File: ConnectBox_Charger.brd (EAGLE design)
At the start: 65 x 30 mm, 1 part, among them J1 CONNECTOR_PI_40_PIN

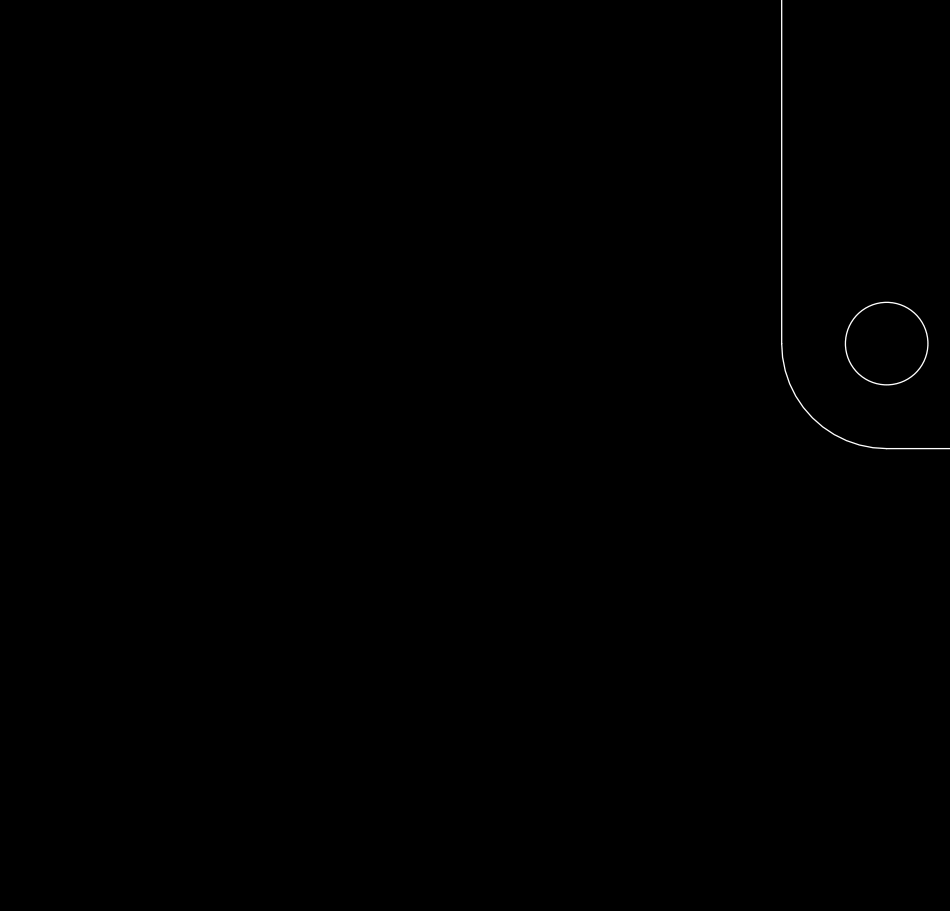
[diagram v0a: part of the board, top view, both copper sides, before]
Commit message: Add LTC4040 Breakout
Breakout from an Analog Devices/Linear Technology LTC4040 “2.5A Battery Backup Power Manager” IC. Boost SMPS with 5V out, and buck SMPS to charge lithium cell. Li-Ion selectable 3.95V/4.0V/4.05V/4.1V Lithium Iron Phosphate LiFePO4 selectable 3.45V/3.5V/3.55V/3.6V

https://www.analog.com/en/products/ltc4040.html
https://www.analog.com/media/en/technical-documentation/data-sheets/4040fb.pdf

Package UFD, QFN 4mm x 5mm. 24 pins plus Exposed Pad. LTC4040EUFD
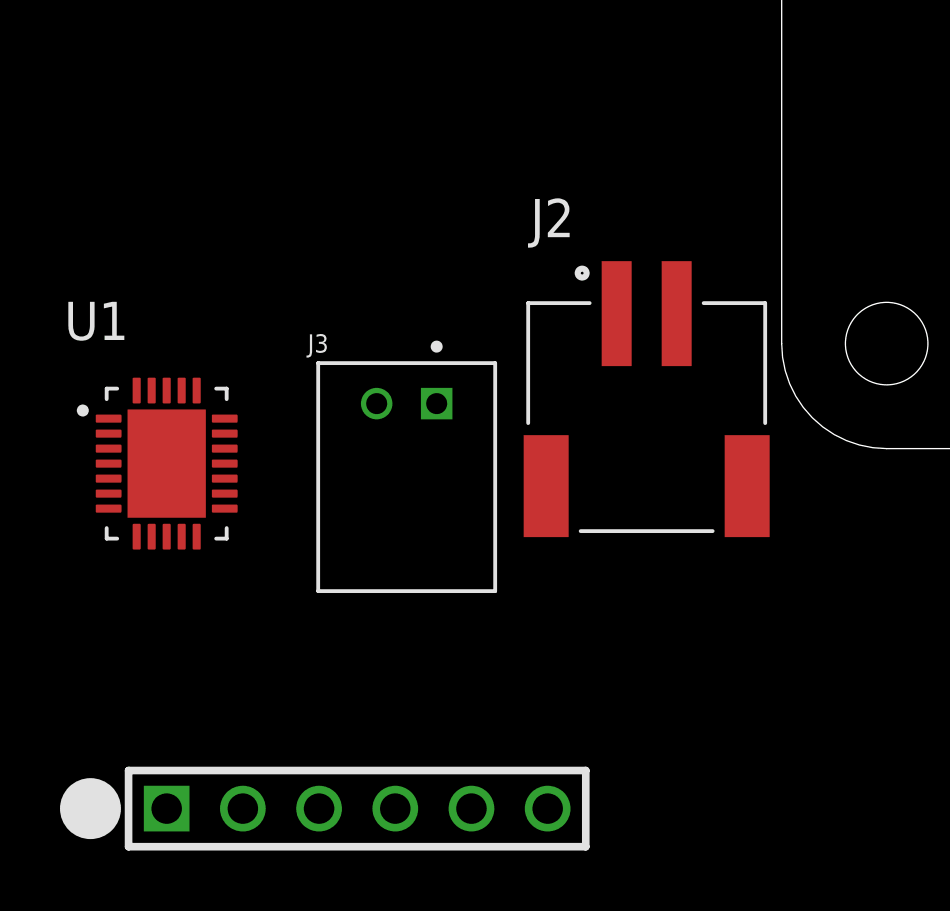
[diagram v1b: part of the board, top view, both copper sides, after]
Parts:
- added J2: JST-2 SMT, ConnectBox_2019:JST_S2B-PH-SM4-TB(LF)(SN)
- added J3: JST-2 TH, ConnectBox_2019:JST_S2B-PH-K-S(LF)(SN)
- added J4: CONNECTOR-6-FTDI, ConnectBox_2019:ESQ-106-XX-X-S
- added U1: LTC4040, ConnectBox_2019:QFN50P500X400X80-25N
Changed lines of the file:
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@@
 <attribute name="VALUE" x="7.1" y="22.055" size="1.27" layer="27"/>
+</element>
+<element name="J2" library="ConnectBox_2019" package="JST_S2B-PH-SM4-TB(LF)(SN)" value="JST-2 SMT" x="-4.5" y="4.5" smashed="yes">
+<attribute name="AVAILABILITY" value="Unavailable" x="-4.5" y="4.5" size="1.778" layer="27" display="off"/>
+<attribute name="DESCRIPTION" value=" PH Series 2 Position 2 mm Pitch Surface Mount Side Entry Shrouded Header " x="-4.5" y="4.5" size="1.778" layer="27" display="off"/>
+<attribute name="MF" value="JST Sales" x="-4.5" y="4.5" size="1.778" layer="27" display="off"/>
+<attribute name="MP" value="S2B-PH-SM4-TB_LF__SN_" x="-4.5" y="4.5" size="1.778" layer="27" display="off"/>
+<attribute name="NAME" x="-8.37423125" y="7.047609375" size="1.27278125" layer="25"/>
+<attribute name="PACKAGE" value="FakePackage u" x="-4.5" y="4.5" size="1.778" layer="27" display="off"/>
+<attribute name="PRICE" value="None" x="-4.5" y="4.5" size="1.778" layer="27" display="off"/>
+<attribute name="VALUE" x="-8.25341875" y="-5.6187" size="1.274540625" layer="27"/>
+</element>
+<element name="J3" library="ConnectBox_2019" package="JST_S2B-PH-K-S(LF)(SN)" value="JST-2 TH" x="-12.5" y="1.5" smashed="yes">
+<attribute name="AVAILABILITY" value="Unavailable" x="-12.5" y="1.5" size="1.778" layer="27" display="off"/>
+<attribute name="DESCRIPTION" value=" PH Series 2 Position 2.0 mm Through Hole Side Entry Shrouded Header " x="-12.5" y="1.5" size="1.778" layer="27" display="off"/>
+<attribute name="MF" value="JST Sales" x="-12.5" y="1.5" size="1.778" layer="27" display="off"/>
+<attribute name="MP" value="S2B-PH-K-S_LF__SN_" x="-12.5" y="1.5" size="1.778" layer="27" display="off"/>
+<attribute name="NAME" x="-15.8" y="3.2" size="0.6096" layer="25"/>
+<attribute name="PACKAGE" value="None" x="-12.5" y="1.5" size="1.778" layer="27" display="off"/>
+<attribute name="PRICE" value="None" x="-12.5" y="1.5" size="1.778" layer="27" display="off"/>
+<attribute name="VALUE" x="-15.8" y="-5.7" size="0.6096" layer="27"/>
+</element>
+<element name="U1" library="ConnectBox_2019" package="QFN50P500X400X80-25N" value="LTC4040" x="-20.5" y="-0.5" smashed="yes">
+<attribute name="NAME" x="-23.91453125" y="3.62046875" size="1.271690625" layer="25"/>
+<attribute name="VALUE" x="-23.91575" y="-4.62193125" size="1.272140625" layer="27" align="top-left"/>
+</element>
+<element name="J4" library="ConnectBox_2019" package="ESQ-106-XX-X-S" value="CONNECTOR-6-FTDI" x="-20.5" y="-12" smashed="yes">
+<attribute name="NAME" x="-14.15" y="-8.19" size="1.524" layer="25" font="vector" ratio="10" align="center"/>
+<attribute name="NAME" x="-14.15" y="-12" size="1.524" layer="51" ratio="10" align="center"/>
+<attribute name="VALUE" x="-14.15" y="-15.81" size="1.524" layer="27" font="vector" ratio="10" align="center"/>
 </element>
 </elements>

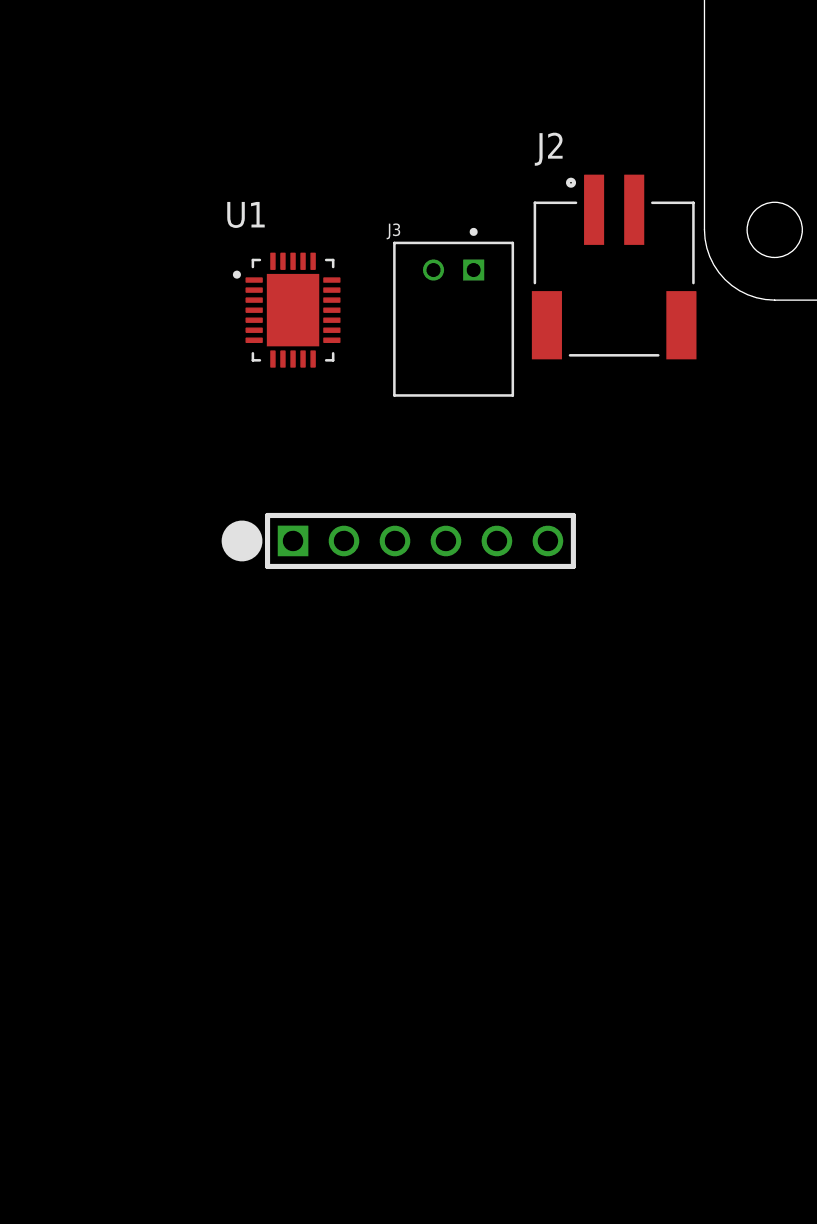
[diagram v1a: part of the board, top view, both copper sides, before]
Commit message: Continue Charger Schematic and Library Parts Add USB A Receptacle, microUSB Power in, decide on SMT for JST-2, start to add nets.
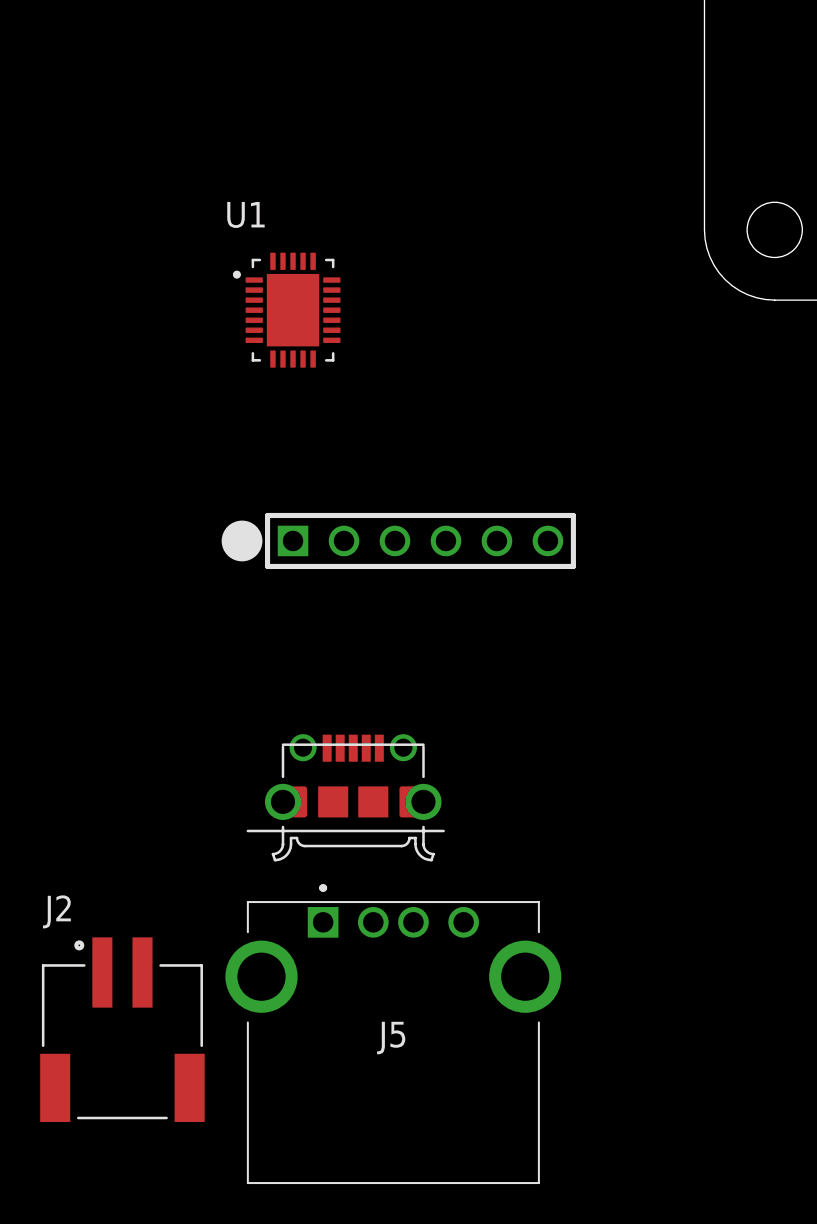
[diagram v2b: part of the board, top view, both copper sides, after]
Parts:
- added J5: 5V Charger Output, ConnectBox_2019:SS52100001
- J2: value JST-2 SMT -> Lithium Cell
- J3: value JST-2 TH -> microUSB Power In; device ConnectBox_2019:JST_S2B-PH-K-S(LF)(SN) -> ConnectBox_2019:FRAMATOME_10118194-0001LF
- J4: value CONNECTOR-6-FTDI -> FTDI Serial
- moved J2 45.2 mm to (-29.0, -33.5)
- moved J3 27.0 mm to (-17.5, -25.0)
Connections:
- new net +5V: J5.1
- new net BATT: J2.1
- new net FROM_PI: J1.8, J4.5
- new net GND: J1.25, J1.39, J1.9, J2.2, J3.5, J4.1, J5.4, J5.MH1, J5.MH2, U1.25
- new net TO_PI: J1.10, J4.4
- new net V_IN: J3.1
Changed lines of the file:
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@@
 <attribute name="VALUE" x="7.1" y="22.055" size="1.27" layer="27"/>
-</element>
-<element name="J2" library="ConnectBox_2019" package="JST_S2B-PH-SM4-TB(LF)(SN)" value="JST-2 SMT" x="-4.5" y="4.5" smashed="yes">
-<attribute name="AVAILABILITY" value="Unavailable" x="-4.5" y="4.5" size="1.778" layer="27" display="off"/>
-<attribute name="DESCRIPTION" value=" PH Series 2 Position 2 mm Pitch Surface Mount Side Entry Shrouded Header " x="-4.5" y="4.5" size="1.778" layer="27" display="off"/>
-<attribute name="MF" value="JST Sales" x="-4.5" y="4.5" size="1.778" layer="27" display="off"/>
-<attribute name="MP" value="S2B-PH-SM4-TB_LF__SN_" x="-4.5" y="4.5" size="1.778" layer="27" display="off"/>
-<attribute name="NAME" x="-8.37423125" y="7.047609375" size="1.27278125" layer="25"/>
-<attribute name="PACKAGE" value="FakePackage u" x="-4.5" y="4.5" size="1.778" layer="27" display="off"/>
-<attribute name="PRICE" value="None" x="-4.5" y="4.5" size="1.778" layer="27" display="off"/>
-<attribute name="VALUE" x="-8.25341875" y="-5.6187" size="1.274540625" layer="27"/>
-</element>
-<element name="J3" library="ConnectBox_2019" package="JST_S2B-PH-K-S(LF)(SN)" value="JST-2 TH" x="-12.5" y="1.5" smashed="yes">
-<attribute name="AVAILABILITY" value="Unavailable" x="-12.5" y="1.5" size="1.778" layer="27" display="off"/>
-<attribute name="DESCRIPTION" value=" PH Series 2 Position 2.0 mm Through Hole Side Entry Shrouded Header " x="-12.5" y="1.5" size="1.778" layer="27" display="off"/>
-<attribute name="MF" value="JST Sales" x="-12.5" y="1.5" size="1.778" layer="27" display="off"/>
-<attribute name="MP" value="S2B-PH-K-S_LF__SN_" x="-12.5" y="1.5" size="1.778" layer="27" display="off"/>
-<attribute name="NAME" x="-15.8" y="3.2" size="0.6096" layer="25"/>
-<attribute name="PACKAGE" value="None" x="-12.5" y="1.5" size="1.778" layer="27" display="off"/>
-<attribute name="PRICE" value="None" x="-12.5" y="1.5" size="1.778" layer="27" display="off"/>
-<attribute name="VALUE" x="-15.8" y="-5.7" size="0.6096" layer="27"/>
 </element>
 <element name="U1" library="ConnectBox_2019" package="QFN50P500X400X80-25N" value="LTC4040" x="-20.5" y="-0.5" smashed="yes">
@@
 <attribute name="VALUE" x="-23.91575" y="-4.62193125" size="1.272140625" layer="27" align="top-left"/>
 </element>
-<element name="J4" library="ConnectBox_2019" package="ESQ-106-XX-X-S" value="CONNECTOR-6-FTDI" x="-20.5" y="-12" smashed="yes">
+<element name="J4" library="ConnectBox_2019" package="ESQ-106-XX-X-S" value="FTDI Serial" x="-20.5" y="-12" smashed="yes">
 <attribute name="NAME" x="-14.15" y="-8.19" size="1.524" layer="25" font="vector" ratio="10" align="center"/>
 <attribute name="NAME" x="-14.15" y="-12" size="1.524" layer="51" ratio="10" align="center"/>
 <attribute name="VALUE" x="-14.15" y="-15.81" size="1.524" layer="27" font="vector" ratio="10" align="center"/>
 </element>
+<element name="J3" library="ConnectBox_2019" package="FRAMATOME_10118194-0001LF" value="microUSB Power In" x="-17.5" y="-25" smashed="yes">
+<attribute name="AVAILABILITY" value="Good" x="-17.5" y="-25" size="1.778" layer="27" display="off"/>
+<attribute name="DESCRIPTION" value="Conn Micro USB Type B RCP 5 POS 0.65mm Solder RA SMD 5 Terminal 1 Port T/R" x="-17.5" y="-25" size="1.778" layer="27" display="off"/>
+<attribute name="MF" value="FCI" x="-17.5" y="-25" size="1.778" layer="27" display="off"/>
+<attribute name="MP" value="10118194-0001LF" x="-17.5" y="-25" size="1.778" layer="27" display="off"/>
+<attribute name="NAME" x="-22" y="-25.9" size="1.27" layer="25" rot="R90"/>
+<attribute name="NAME" x="-17.5" y="-24.365" size="2.54" layer="51" align="center"/>
+<attribute name="PACKAGE" value="DIP-4 FCI" x="-17.5" y="-25" size="1.778" layer="27" display="off"/>
+<attribute name="PRICE" value="0.24 USD" x="-17.5" y="-25" size="1.778" layer="27" display="off"/>
+<attribute name="VALUE" x="-11.6" y="-24.9" size="1.27" layer="27" rot="R90"/>
+</element>
+<element name="J5" library="ConnectBox_2019" package="SS52100001" value="5V Charger Output" x="-19" y="-31" smashed="yes">
+<attribute name="DESCRIPTION" value="STEWART CONNECTOR - SS-52100-001 - USB CONN, 2.0 TYPE A, RCPT, 4POS, TH" x="-19" y="-31" size="1.778" layer="27" display="off"/>
+<attribute name="HEIGHT" value="6.9mm" x="-19" y="-31" size="1.778" layer="27" display="off"/>
+<attribute name="MANUFACTURER_NAME" value="Bel-Stewart" x="-19" y="-31" size="1.778" layer="27" display="off"/>
+<attribute name="MANUFACTURER_PART_NUMBER" value="SS-52100-001" x="-19" y="-31" size="1.778" layer="27" display="off"/>
+<attribute name="MOUSER_PART_NUMBER" value="530-SS-52100-001" x="-19" y="-31" size="1.778" layer="27" display="off"/>
+<attribute name="MOUSER_PRICE-STOCK" value="https://www.mouser.com/Search/Refine.aspx?Keyword=530-SS-52100-001" x="-19" y="-31" size="1.778" layer="27" display="off"/>
+<attribute name="NAME" x="-15.5" y="-36.59" size="1.27" layer="25" align="center"/>
+<attribute name="RS_PART_NUMBER" value="" x="-19" y="-31" size="1.778" layer="27" display="off"/>
+<attribute name="RS_PRICE-STOCK" value="" x="-19" y="-31" size="1.778" layer="27" display="off"/>
+<attribute name="VALUE" x="-15.5" y="-36.59" size="1.27" layer="27" align="center"/>
+</element>
+<element name="J2" library="ConnectBox_2019" package="JST_S2B-PH-SM4-TB(LF)(SN)" value="Lithium Cell" x="-29" y="-33.5" smashed="yes">
+<attribute name="AVAILABILITY" value="Unavailable" x="-29" y="-33.5" size="1.778" layer="27" display="off"/>
+<attribute name="DESCRIPTION" value=" PH Series 2 Position 2 mm Pitch Surface Mount Side Entry Shrouded Header " x="-29" y="-33.5" size="1.778" layer="27" display="off"/>
+<attribute name="MF" value="JST Sales" x="-29" y="-33.5" size="1.778" layer="27" display="off"/>
+<attribute name="MP" value="S2B-PH-SM4-TB_LF__SN_" x="-29" y="-33.5" size="1.778" layer="27" display="off"/>
+<attribute name="NAME" x="-32.87423125" y="-30.952390625" size="1.27278125" layer="25"/>
+<attribute name="PACKAGE" value="FakePackage u" x="-29" y="-33.5" size="1.778" layer="27" display="off"/>
+<attribute name="PRICE" value="None" x="-29" y="-33.5" size="1.778" layer="27" display="off"/>
+<attribute name="VALUE" x="-32.75341875" y="-43.6187" size="1.274540625" layer="27"/>
+</element>
 </elements>
 <signals>
+<signal name="GND">
+<contactref element="J4" pad="1"/>
+<contactref element="J1" pad="39"/>
+<contactref element="J1" pad="25"/>
+<contactref element="J1" pad="9"/>
+<contactref element="U1" pad="25"/>
+<contactref element="J3" pad="5"/>
+<contactref element="J5" pad="MH2" route="any" routetag="G$1.SHIELD"/>
+<contactref element="J5" pad="MH1" route="any" routetag="G$1.SHIELD"/>
+<contactref element="J5" pad="4"/>
+<contactref element="J2" pad="2"/>
+<wire x1="38.85" y1="25.23" x2="56.63" y2="25.23" width="0" layer="19" extent="1-1"/>
+<wire x1="18.53" y1="25.23" x2="38.85" y2="25.23" width="0" layer="19" extent="1-1"/>
+<wire x1="-20.5" y1="-0.5" x2="18.53" y2="25.23" width="0" layer="19" extent="1-1"/>
+<wire x1="-20.5" y1="-12" x2="-20.5" y2="-0.5" width="0" layer="19" extent="1-1"/>
+<wire x1="-16.2" y1="-22.325" x2="-20.5" y2="-12" width="0" layer="19" extent="1-1"/>
+<wire x1="-12" y1="-31" x2="-16.2" y2="-22.325" width="0" layer="19" extent="1-1"/>
+<wire x1="-8.93" y1="-33.71" x2="-12" y2="-31" width="0" layer="19" extent="1-1"/>
+<wire x1="-28" y1="-33.5" x2="-22.07" y2="-33.71" width="0" layer="19" extent="1-1"/>
+</signal>
+<signal name="TO_PI">
+<contactref element="J4" pad="4"/>
+<contactref element="J1" pad="10"/>
+<wire x1="-12.88" y1="-12" x2="18.53" y2="27.77" width="0" layer="19" extent="1-1"/>
+</signal>
+<signal name="FROM_PI">
+<contactref element="J4" pad="5"/>
+<contactref element="J1" pad="8"/>
+<wire x1="-10.34" y1="-12" x2="15.99" y2="27.77" width="0" layer="19" extent="1-1"/>
+</signal>
+<signal name="V_IN">
+<contactref element="J3" pad="1"/>
+</signal>
+<signal name="+5V">
+<contactref element="J5" pad="1"/>
+</signal>
+<signal name="BATT">
+<contactref element="J2" pad="1"/>
+</signal>
 </signals>
 <mfgpreviewcolors>
